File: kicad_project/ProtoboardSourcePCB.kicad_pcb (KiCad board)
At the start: 2 copper layers, 10 parts, among them J1 Conn_01x05, J2 Conn_01x05, J3 Conn_01x05, J4 Conn_01x05

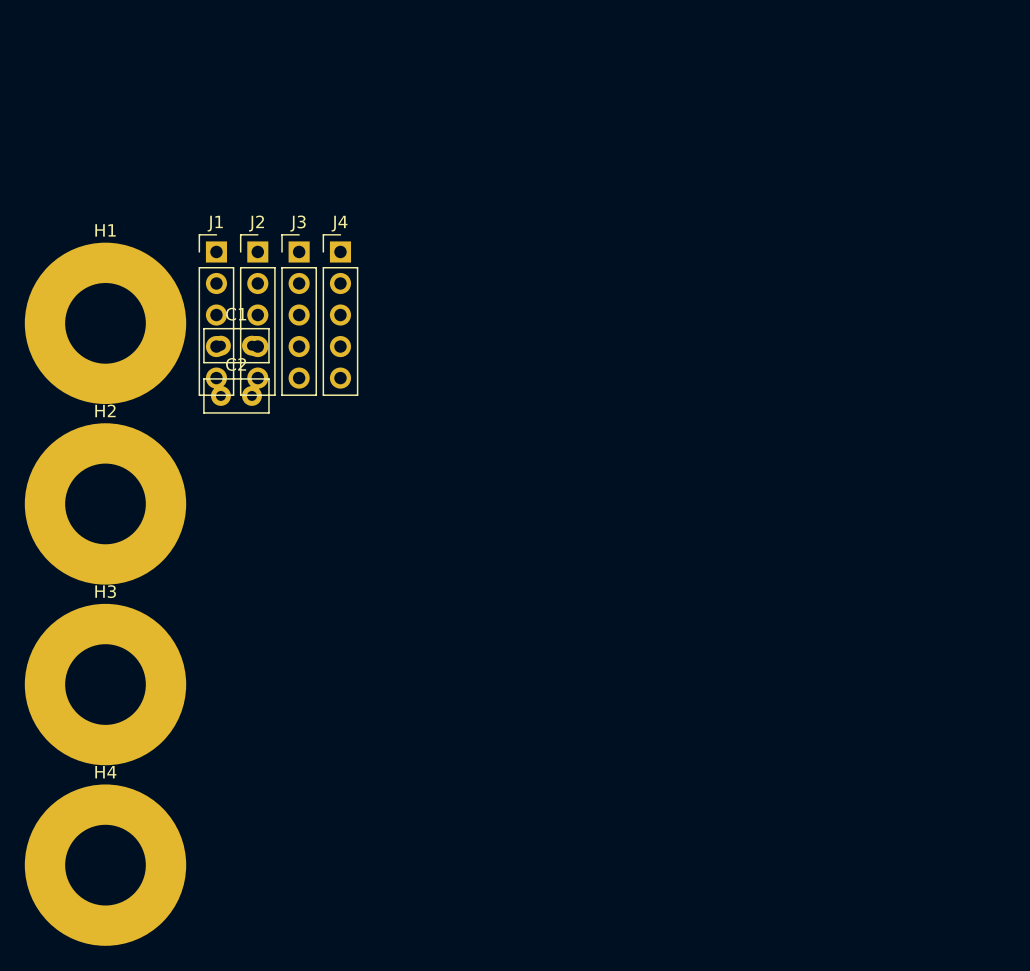
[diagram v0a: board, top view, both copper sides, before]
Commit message: Corrigiendo huellas, colocando componentes y delimitando espacio de la PCB
Signed-off-by: RoMadrigal <rmadrigalmontes@gmail.com>
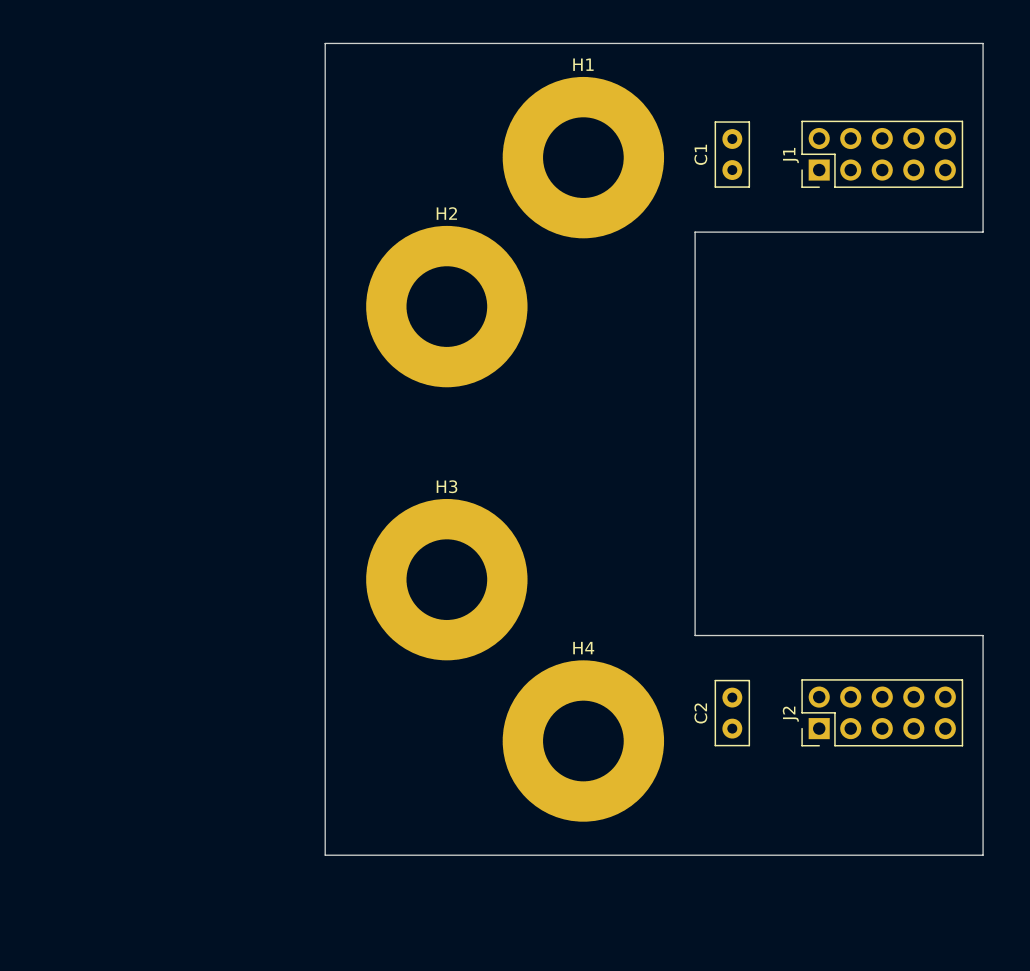
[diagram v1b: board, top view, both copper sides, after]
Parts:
- removed J3, J4: Conn_01x05, Connector_PinHeader_2.54mm:PinHeader_1x05_P2.54mm_Vertical
- J1, J2: value Conn_01x05 -> Conn_02x05_Odd_Even; footprint Connector_PinHeader_2.54mm:PinHeader_1x05_P2.54mm_Vertical -> Connector_PinHeader_2.54mm:PinHeader_2x05_P2.54mm_Vertical
- moved J2 59.3 mm to (150.0, 95.0), turned to 90 degrees
- moved C2 49.1 mm to (143.0, 95.0), turned to 90 degrees
- moved J1 49.0 mm to (150.0, 50.0), turned to 90 degrees
- moved C1 43.6 mm to (143.0, 50.0), turned to 90 degrees
- moved H1 40.7 mm to (131.0, 49.0)
- moved H4 39.8 mm to (131.0, 96.0)
- moved H2 31.8 mm to (120.0, 61.0)
- moved H3 28.8 mm to (120.0, 83.0)
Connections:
- J1 pad 1: VCC -> GND1
- J1 pad 3: VCC -> GND1
- J1 pad 5: VCC -> GND1
- J2 pad 1: GND1 -> GND2
- J2 pad 2: GND1 -> VDD
- J2 pad 3: GND1 -> GND2
- J2 pad 4: GND1 -> VDD
- J2 pad 5: GND1 -> GND2
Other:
- board outline added: 53 x 65.4 mm

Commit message: Modificando huella de los capacitores y reacomodando componentes
Signed-off-by: RoMadrigal <rmadrigalmontes@gmail.com>
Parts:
- C1, C2: footprint Capacitor_THT:C_Disc_D5.0mm_W2.5mm_P2.50mm -> Capacitor_SMD:C_1206_3216Metric_Pad1.33x1.80mm_HandSolder
- moved C2 1.20 mm to (143.0, 93.8)
- moved C1 1.10 mm to (143.0, 48.9)

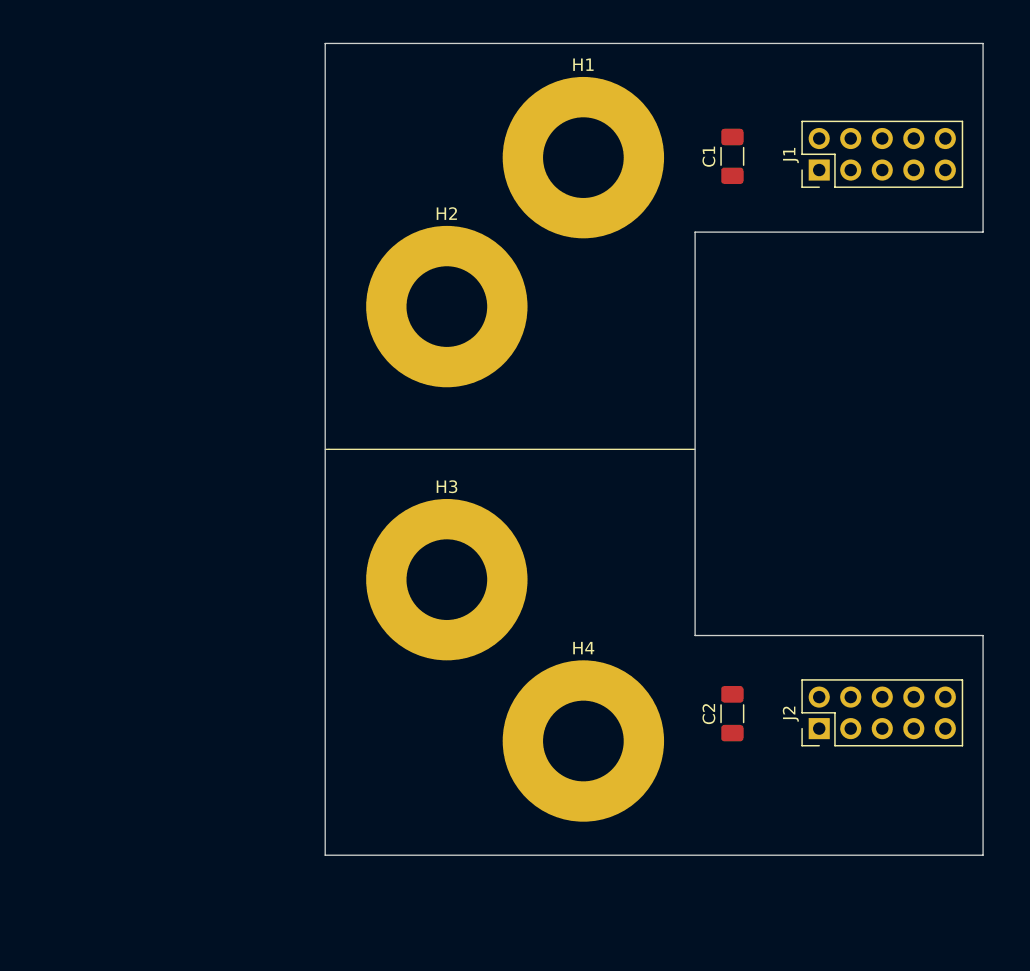
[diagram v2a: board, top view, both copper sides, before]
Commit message: Modificando dimensiones de la PCB y agregando texto en Silkscreen
Signed-off-by: RoMadrigal <rmadrigalmontes@gmail.com>
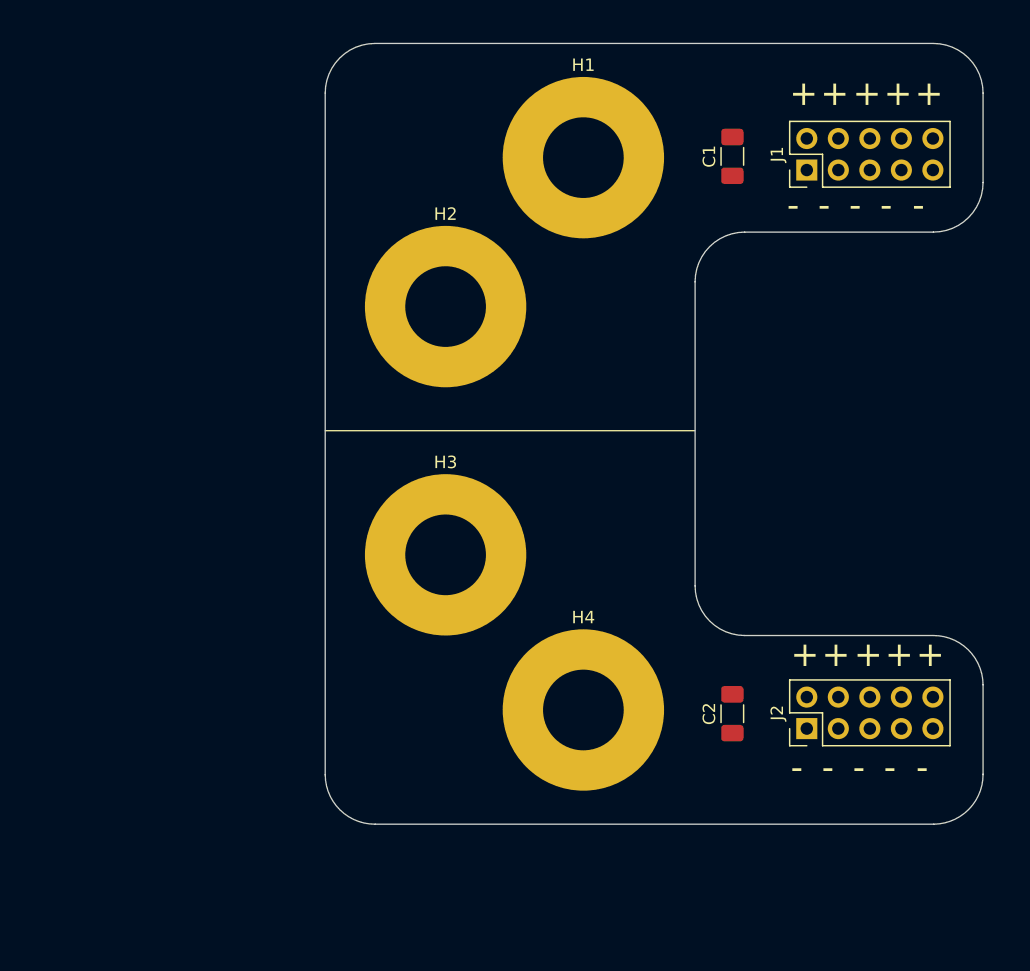
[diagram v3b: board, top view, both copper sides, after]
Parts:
- moved H4 2.50 mm to (131.0, 93.5)
- moved H3 2.00 mm to (119.9, 81.0)
- moved J1 1.00 mm to (149.0, 50.0)
- moved J2 1.00 mm to (149.0, 95.0)
- moved H2 0.10 mm to (119.9, 61.0)
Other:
- board size 53 x 65.4 mm -> 53 x 62.9 mm
- board text added: "+"
- board text added: "-"

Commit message: Agregando agujeros de montaje en la PCB
Signed-off-by: RoMadrigal <rmadrigalmontes@gmail.com>
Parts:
- added REF**: MountingHole_3.2mm_M3, MountingHole:MountingHole_3.2mm_M3, F.Cu at (116.0, 96.9)
- added REF**: MountingHole_3.2mm_M3, MountingHole:MountingHole_3.2mm_M3, F.Cu at (116.0, 45.6)
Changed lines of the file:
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@@
 	(net 3 "VDD")
 	(net 4 "GND2")
+	(footprint "MountingHole:MountingHole_3.2mm_M3"
+		(layer "F.Cu")
+		(at 116 96.9)
+		(descr "Mounting Hole 3.2mm, M3, no annular, generated by kicad-footprint-generator mountinghole.py")
+		(tags "mountinghole M3")
+		(property "Reference" "REF**"
+			(at 0 -4.15 0)
+			(layer "F.SilkS")
+			(hide yes)
+			(effects
+				(font
+					(size 1 1)
+					(thickness 0.15)
+				)
+			)
+		)
+		(property "Value" "MountingHole_3.2mm_M3"
+			(at 0 4.15 0)
+			(layer "F.Fab")
+			(effects
+				(font
+					(size 1 1)
+					(thickness 0.15)
+				)
+			)
+		)
+		(property "Datasheet" ""
+			(at 0 0 0)
+			(layer "F.Fab")
+			(hide yes)
+			(effects
+				(font
+					(size 1.27 1.27)
+					(thickness 0.15)
+				)
+			)
+		)
+		(property "Description" ""
+			(at 0 0 0)
+			(layer "F.Fab")
+			(hide yes)
+			(effects
+				(font
+					(size 1.27 1.27)
+					(thickness 0.15)
+				)
+			)
+		)
+		(attr exclude_from_pos_files exclude_from_bom)
+		(fp_circle
+			(center 0 0)
+			(end 3.2 0)
+			(stroke
+				(width 0.15)
+				(type solid)
+			)
+			(fill no)
+			(layer "Cmts.User")
+		)
+		(fp_circle
+			(center 0 0)
+			(end 3.45 0)
+			(stroke
+				(width 0.05)
+				(type solid)
+			)
+			(fill no)
+			(layer "F.CrtYd")
+		)
+		(fp_text user "${REFERENCE}"
+			(at 0 0 0)
+			(layer "F.Fab")
+			(effects
+				(font
+					(size 1 1)
+					(thickness 0.15)
+				)
+			)
+		)
+		(pad "" np_thru_hole circle
+			(at 0 0)
+			(size 3.2 3.2)
+			(drill 3.2)
+			(layers "*.Cu" "*.Mask")
+		)
+		(embedded_fonts no)
+	)
+	(footprint "MountingHole:MountingHole_3.2mm_M3"
+		(layer "F.Cu")
+		(at 116 45.6)
+		(descr "Mounting Hole 3.2mm, M3, no annular, generated by kicad-footprint-generator mountinghole.py")
+		(tags "mountinghole M3")
+		(property "Reference" "REF**"
+			(at 0 -4.15 0)
+			(layer "F.SilkS")
+			(hide yes)
+			(effects
+				(font
+					(size 1 1)
+					(thickness 0.15)
+				)
+			)
+		)
+		(property "Value" "MountingHole_3.2mm_M3"
+			(at 0 4.15 0)
+			(layer "F.Fab")
+			(effects
+				(font
+					(size 1 1)
+					(thickness 0.15)
+				)
+			)
+		)
+		(property "Datasheet" ""
+			(at 0 0 0)
+			(layer "F.Fab")
+			(hide yes)
+			(effects
+				(font
+					(size 1.27 1.27)
+					(thickness 0.15)
+				)
+			)
+		)
+		(property "Description" ""
+			(at 0 0 0)
+			(layer "F.Fab")
+			(hide yes)
+			(effects
+				(font
+					(size 1.27 1.27)
+					(thickness 0.15)
+				)
+			)
+		)
+		(attr exclude_from_pos_files exclude_from_bom)
+		(fp_circle
+			(center 0 0)
+			(end 3.2 0)
+			(stroke
+				(width 0.15)
+				(type solid)
+			)
+			(fill no)
+			(layer "Cmts.User")
+		)
+		(fp_circle
+			(center 0 0)
+			(end 3.45 0)
+			(stroke
+				(width 0.05)
+				(type solid)
+			)
+			(fill no)
+			(layer "F.CrtYd")
+		)
+		(fp_text user "${REFERENCE}"
+			(at 0 0 0)
+			(layer "F.Fab")
+			(effects
+				(font
+					(size 1 1)
+					(thickness 0.15)
+				)
+			)
+		)
+		(pad "" np_thru_hole circle
+			(at 0 0)
+			(size 3.2 3.2)
+			(drill 3.2)
+			(layers "*.Cu" "*.Mask")
+		)
+		(embedded_fonts no)
+	)
 	(footprint "Capacitor_SMD:C_1206_3216Metric_Pad1.33x1.80mm_HandSolder"
 		(layer "F.Cu")

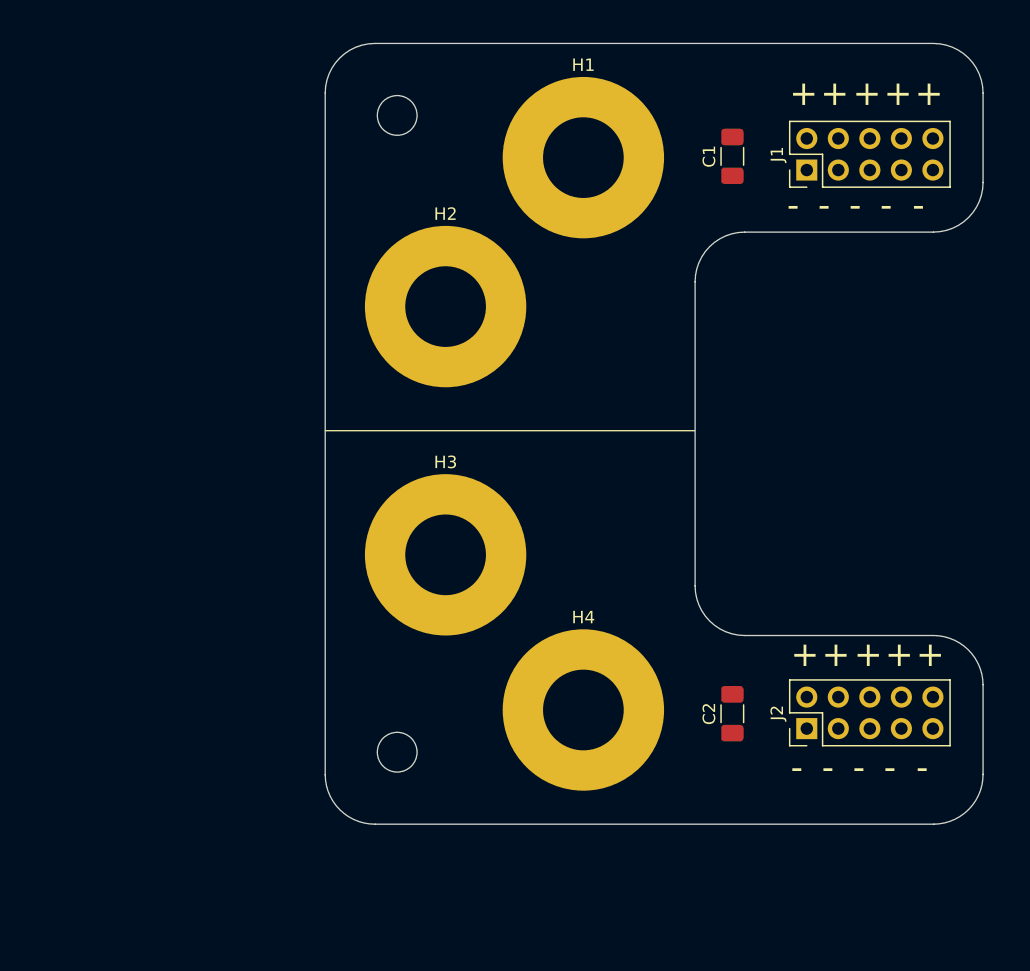
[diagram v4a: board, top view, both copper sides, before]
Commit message: Definiendo los planos de tierra y alimentacion, y agregando vias para los capacitores
Signed-off-by: RoMadrigal <rmadrigalmontes@gmail.com>
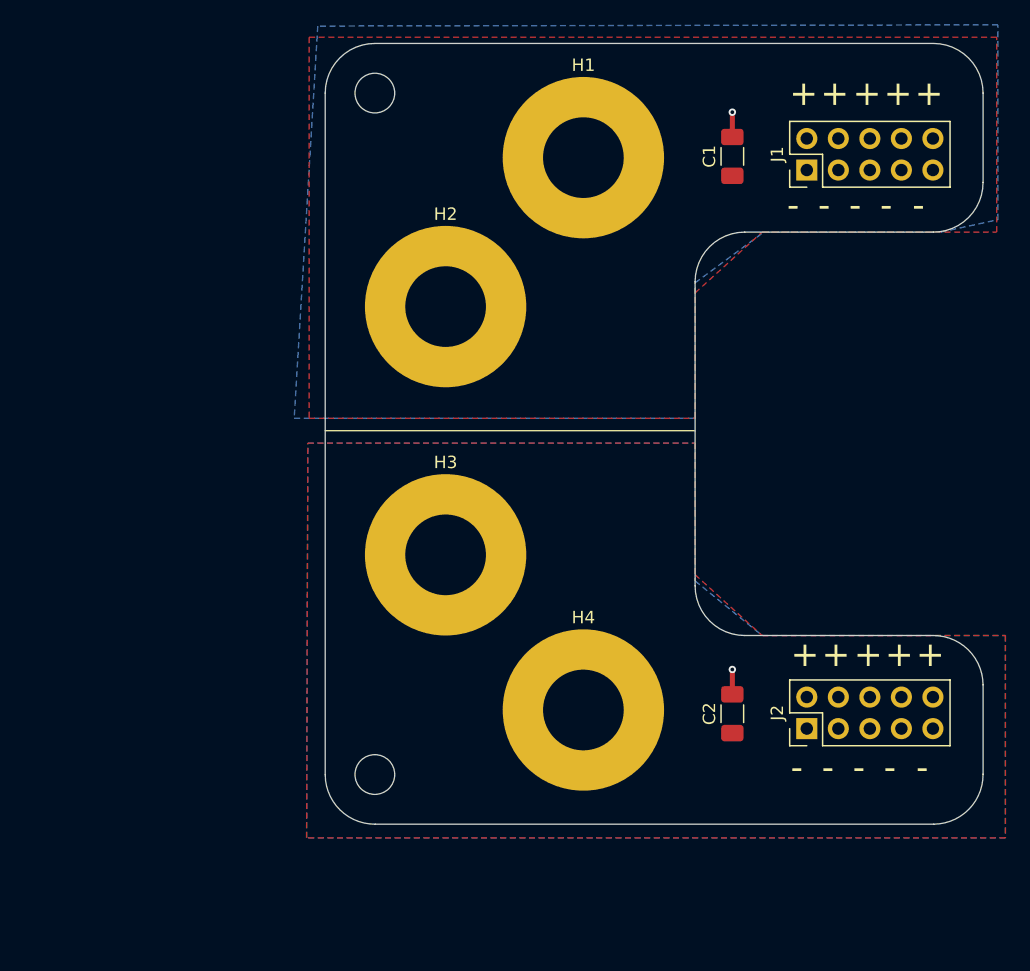
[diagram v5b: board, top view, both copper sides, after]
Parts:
- moved REF** 2.55 mm to (114.2, 43.8)
- moved REF** 2.55 mm to (114.2, 98.7)
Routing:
- net GND2: track 0.00 -> 2.00 mm, vias 0 -> 1
- net GND1: track 0.00 -> 2.00 mm, vias 0 -> 1
- added copper zone on B.Cu, net GND1
- added copper zone on B.Cu, net GND2
- added copper zone on F.Cu, net VCC
- added copper zone on F.Cu, net VDD
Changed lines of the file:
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@@
 	(footprint "MountingHole:MountingHole_3.2mm_M3"
 		(layer "F.Cu")
-		(at 116 96.9)
+		(at 114.2 98.7)
 		(descr "Mounting Hole 3.2mm, M3, no annular, generated by kicad-footprint-generator mountinghole.py")
 		(tags "mountinghole M3")
@@
 	(footprint "MountingHole:MountingHole_3.2mm_M3"
 		(layer "F.Cu")
-		(at 116 45.6)
+		(at 114.2 43.8)
 		(descr "Mounting Hole 3.2mm, M3, no annular, generated by kicad-footprint-generator mountinghole.py")
 		(tags "mountinghole M3")
@@
 		(layer "F.SilkS")
 	)
+	(gr_line
+		(start 109.7 72)
+		(end 142.2 72)
+		(stroke
+			(width 0.1)
+			(type default)
+		)
+		(layer "Dwgs.User")
+	)
+	(gr_line
+		(start 109.7 70)
+		(end 140.8 70)
+		(stroke
+			(width 0.1)
+			(type default)
+		)
+		(layer "Dwgs.User")
+	)
 	(gr_arc
 		(start 159.2 39.8)
@@
 		)
 	)
+	(segment
+		(start 143 45.3375)
+		(end 143 47.3375)
+		(width 0.4)
+		(layer "F.Cu")
+		(net 1)
+	)
+	(via
+		(at 143 45.3375)
+		(size 0.6)
+		(drill 0.3)
+		(layers "F.Cu" "B.Cu")
+		(net 1)
+	)
+	(segment
+		(start 143 90.2375)
+		(end 143 92.2375)
+		(width 0.4)
+		(layer "F.Cu")
+		(net 4)
+	)
+	(via
+		(at 143 90.2375)
+		(size 0.6)
+		(drill 0.3)
+		(layers "F.Cu" "B.Cu")
+		(net 4)
+	)
+	(zone
+		(net 2)
+		(net_name "VCC")
+		(layer "F.Cu")
+		(hatch edge 0.5)
+		(priority 2)
+		(connect_pads
+			(clearance 0.5)
+		)
+		(min_thickness 0.25)
+		(filled_areas_thickness no)
+		(fill yes
+			(thermal_gap 0.5)
+			(thermal_bridge_width 0.5)
+		)
+		(polygon
+			(pts
+				(xy 140 70) (xy 140 59.9) (xy 145.4 55) (xy 164.3 55) (xy 164.3 39.3) (xy 108.9 39.3) (xy 108.9 70)
+			)
+		)
+	)
+	(zone
+		(net 3)
+		(net_name "VDD")
+		(layer "F.Cu")
+		(hatch edge 0.5)
+		(priority 3)
+		(connect_pads
+			(clearance 0.5)
+		)
+		(min_thickness 0.25)
+		(filled_areas_thickness no)
+		(fill yes
+			(thermal_gap 0.5)
+			(thermal_bridge_width 0.5)
+		)
+		(polygon
+			(pts
+				(xy 140 72) (xy 140 82.6) (xy 145.4 87.5) (xy 165 87.5) (xy 165 103.8) (xy 108.7 103.8) (xy 108.8 72)
+			)
+		)
+	)
+	(zone
+		(net 4)
+		(net_name "GND2")
+		(layer "B.Cu")
+		(hatch edge 0.5)
+		(priority 1)
+		(connect_pads
+			(clearance 0.5)
+		)
+		(min_thickness 0.25)
+		(filled_areas_thickness no)
+		(fill yes
+			(thermal_gap 0.5)
+			(thermal_bridge_width 0.5)
+		)
+		(polygon
+			(pts
+				(xy 140 72) (xy 140 83.1) (xy 145.4 87.5) (xy 165 87.5) (xy 165 103.8) (xy 108.7 103.8) (xy 108.8 72)
+			)
+		)
+	)
+	(zone
+		(net 1)
+		(net_name "GND1")
+		(layer "B.Cu")
+		(hatch edge 0.5)
+		(connect_pads
+			(clearance 0.5)
+		)
+		(min_thickness 0.25)
+		(filled_areas_thickness no)
+		(fill yes
+			(thermal_gap 0.5)
+			(thermal_bridge_width 0.5)
+		)
+		(polygon
+			(pts
+				(xy 140 70) (xy 140 59.087693) (xy 145.535418 55) (xy 159.8 55) (xy 164.4 54) (xy 164.4 38.3) (xy 109.6 38.4)
+				(xy 107.7 70)
+			)
+		)
+	)
